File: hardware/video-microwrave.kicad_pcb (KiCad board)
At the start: 2 copper layers, 66 x 101.6 mm, 85 parts, among them J501 PJ301M-12, J502 PJ301M-12, J503 PJ301M-12, J504 PJ301M-12, J505 PJ301M-12, J506 PJ301M-12, J507 PJ301M-12, J508 PJ301M-12, P101 CONN_01X05, P102 CONN_01X05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

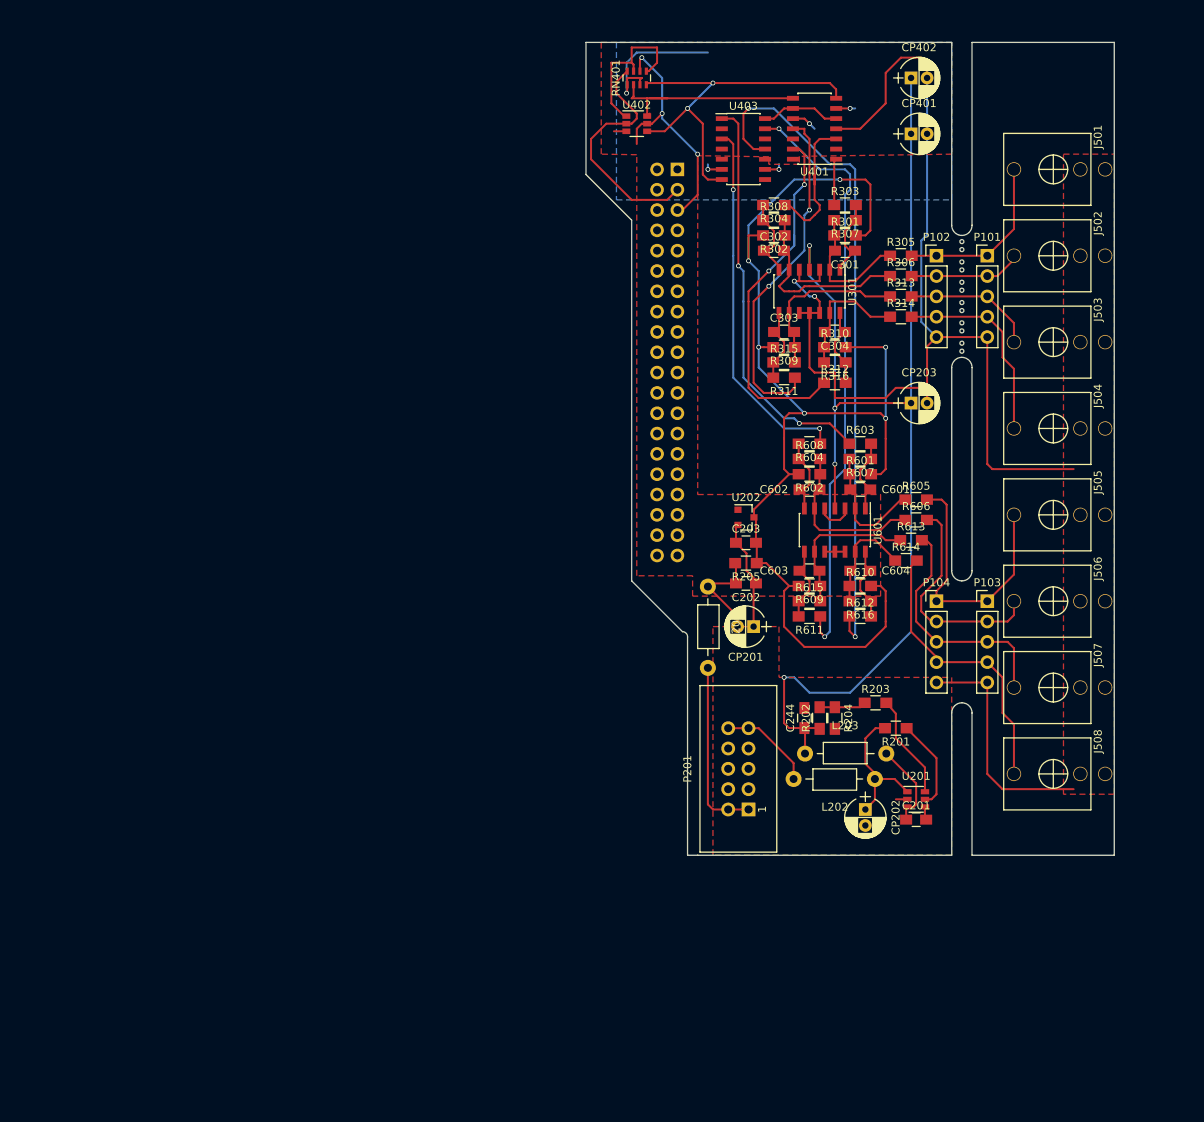
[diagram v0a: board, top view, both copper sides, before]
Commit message: moving footprints to fit real world dimensions
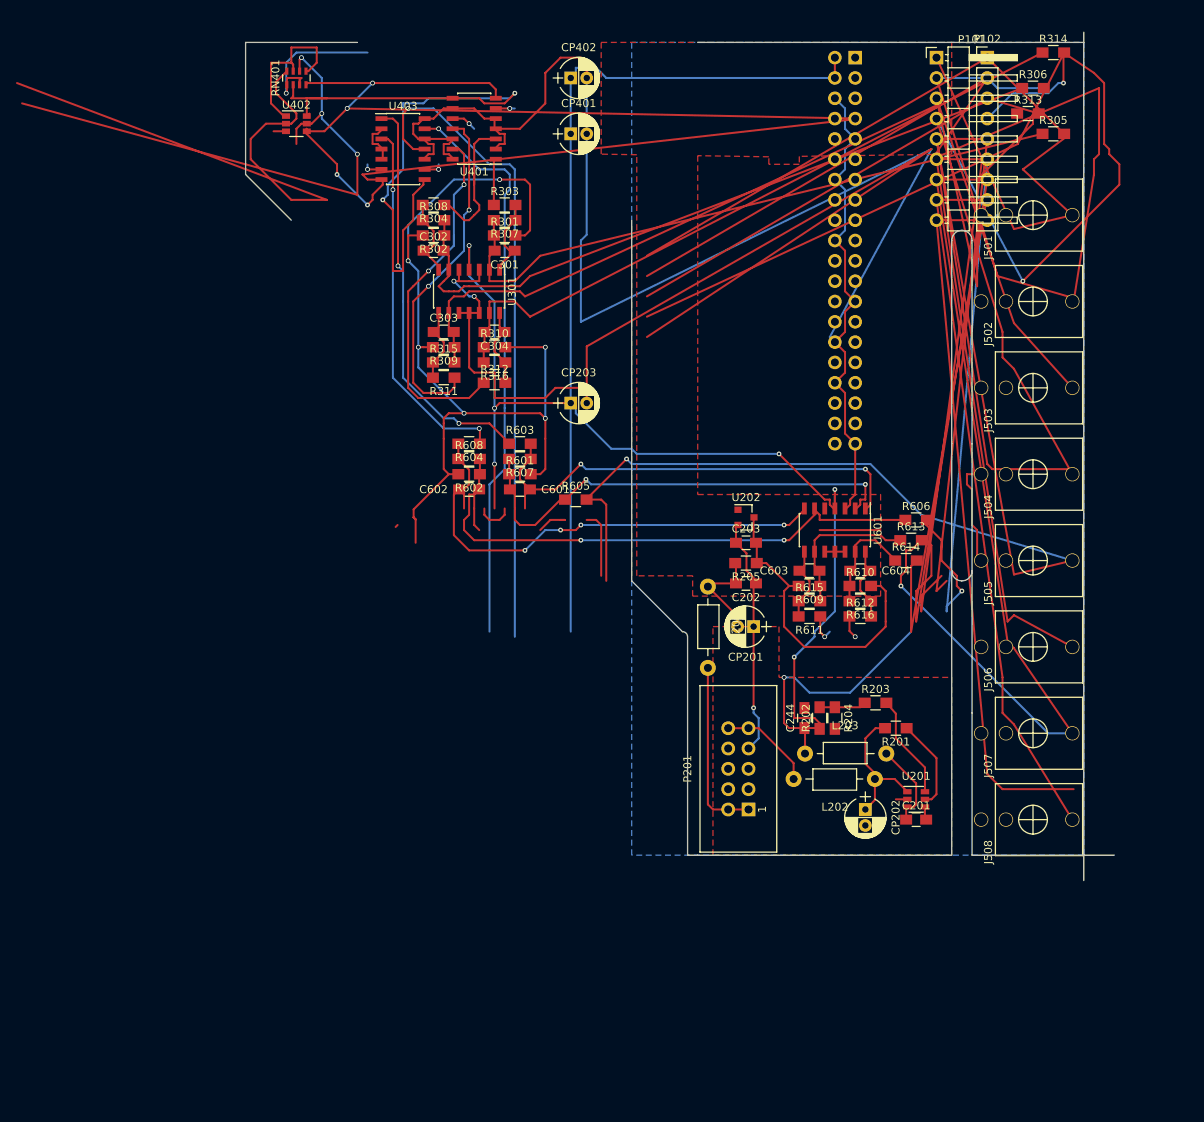
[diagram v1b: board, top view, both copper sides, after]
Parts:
- removed MOUSEBITE1mm (x6): VAL**, Microwrave:Mousebite_Mini_1mm
- removed P103, P104: CONN_01X05, Pin_Headers:Pin_Header_Straight_1x05_Pitch2.54mm
- P101: value CONN_01X05 -> CONN_01X09; footprint Pin_Headers:Pin_Header_Straight_1x05_Pitch2.54mm -> Pin_Headers:Pin_Header_Angled_1x09_Pitch2.54mm
- P102: value CONN_01X05 -> CONN_01X09; footprint Pin_Headers:Pin_Header_Straight_1x05_Pitch2.54mm -> Pin_Headers:Pin_Header_Straight_1x09_Pitch2.54mm
- moved C302 42.5 mm to (87.6, 64.1)
- moved R302 42.5 mm to (87.6, 62.2)
- moved R304 42.5 mm to (87.6, 58.4)
- moved R308 42.5 mm to (87.6, 60.3)
- moved R605 42.5 mm to (105.4, 95.2)
- moved C301 42.5 mm to (96.5, 64.1)
- moved C601 42.5 mm to (98.4, 94.0)
- moved C602 42.5 mm to (92.1, 94.0)
- moved R301 42.5 mm to (96.5, 62.2)
- moved R303 42.5 mm to (96.5, 58.4)
- moved R307 42.5 mm to (96.5, 60.3)
- moved R601 42.5 mm to (98.4, 92.1)
- moved R602 42.5 mm to (92.1, 92.1)
- moved R603 42.5 mm to (98.4, 88.3)
- moved R604 42.5 mm to (92.1, 88.3)
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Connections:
- P101 pad 5: Earth -> /cv5_raw
- P102 pad 5: Earth -> /cv5_raw
- U101 pad 10: Net-(U101-Pad10) -> (no net)
- U101 pad 11: Net-(U101-Pad11) -> (no net)
- U101 pad 12: Net-(U101-Pad12) -> (no net)
- U101 pad 13: Net-(U101-Pad13) -> (no net)
- U101 pad 15: Net-(U101-Pad15) -> (no net)
- U101 pad 16: Net-(U101-Pad16) -> (no net)
- U101 pad 17: Net-(U101-Pad17) -> (no net)
- U101 pad 18: Net-(U101-Pad18) -> (no net)
- U101 pad 19: Net-(U101-Pad19) -> (no net)
- U101 pad 21: Net-(U101-Pad21) -> (no net)
- U101 pad 22: Net-(U101-Pad22) -> (no net)
- U101 pad 23: Net-(U101-Pad23) -> (no net)
- U101 pad 24: Net-(U101-Pad24) -> (no net)
- U101 pad 26: Net-(U101-Pad26) -> (no net)
- U101 pad 27: Net-(U101-Pad27) -> (no net)
- U101 pad 28: Net-(U101-Pad28) -> (no net)
- U101 pad 29: Net-(U101-Pad29) -> (no net)
- U101 pad 31: Net-(U101-Pad31) -> (no net)
- U101 pad 32: Net-(U101-Pad32) -> (no net)
- U101 pad 33: Net-(U101-Pad33) -> (no net)
- U101 pad 35: Net-(U101-Pad35) -> (no net)
- U101 pad 36: Net-(U101-Pad36) -> (no net)
- U101 pad 37: Net-(U101-Pad37) -> (no net)
- U101 pad 38: Net-(U101-Pad38) -> (no net)
- U101 pad 40: Net-(U101-Pad40) -> (no net)
- U101 pad 7: Net-(U101-Pad7) -> (no net)
- U101 pad 8: Net-(U101-Pad8) -> (no net)
- U202 pad 1: Net-(U202-Pad1) -> (no net)
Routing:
- net Earth: track 197.4 -> 505.3 mm, vias 2 -> 3
- net /cv6_raw: track 28.1 -> 243.3 mm, vias 0 -> 1
- net /cv5_raw: track 33.8 -> 247.9 mm, vias 0 -> 1
- net /cv3_raw: track 16.5 -> 202.7 mm
- net /cv4_raw: track 24.8 -> 198.5 mm, vias 0 -> 2
- net /cv7_raw: track 30.3 -> 181.7 mm, vias 0 -> 1
- net /adc/SDA_5V: track 47.7 -> 182.5 mm, vias 2 -> 4
- net /cv8_raw: track 36.0 -> 152.3 mm
- net +5V: track 179.2 -> 292.9 mm, vias 9 -> 12
- net /cv2_raw: track 14.1 -> 126.6 mm
- net /cv1_raw: track 21.6 -> 109.3 mm
- net Net-(C304-Pad2): track 16.3 -> 85.9 mm
- net Net-(C301-Pad2): track 16.8 -> 80.2 mm
- net Net-(C302-Pad2): track 24.3 -> 87.7 mm
- net /adc/SCL_5V: track 26.8 -> 86.4 mm, vias 0 -> 2
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- added copper zone on F.Cu, net +5V
- added copper zone on B.Cu, net Earth
- removed copper zone on B.Cu, net +5V
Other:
- board size 66 x 101.6 mm -> 108.6 x 106 mm

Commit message: made space for an expansion connector. net needs updating for 8 100k resistors coming from raw signals
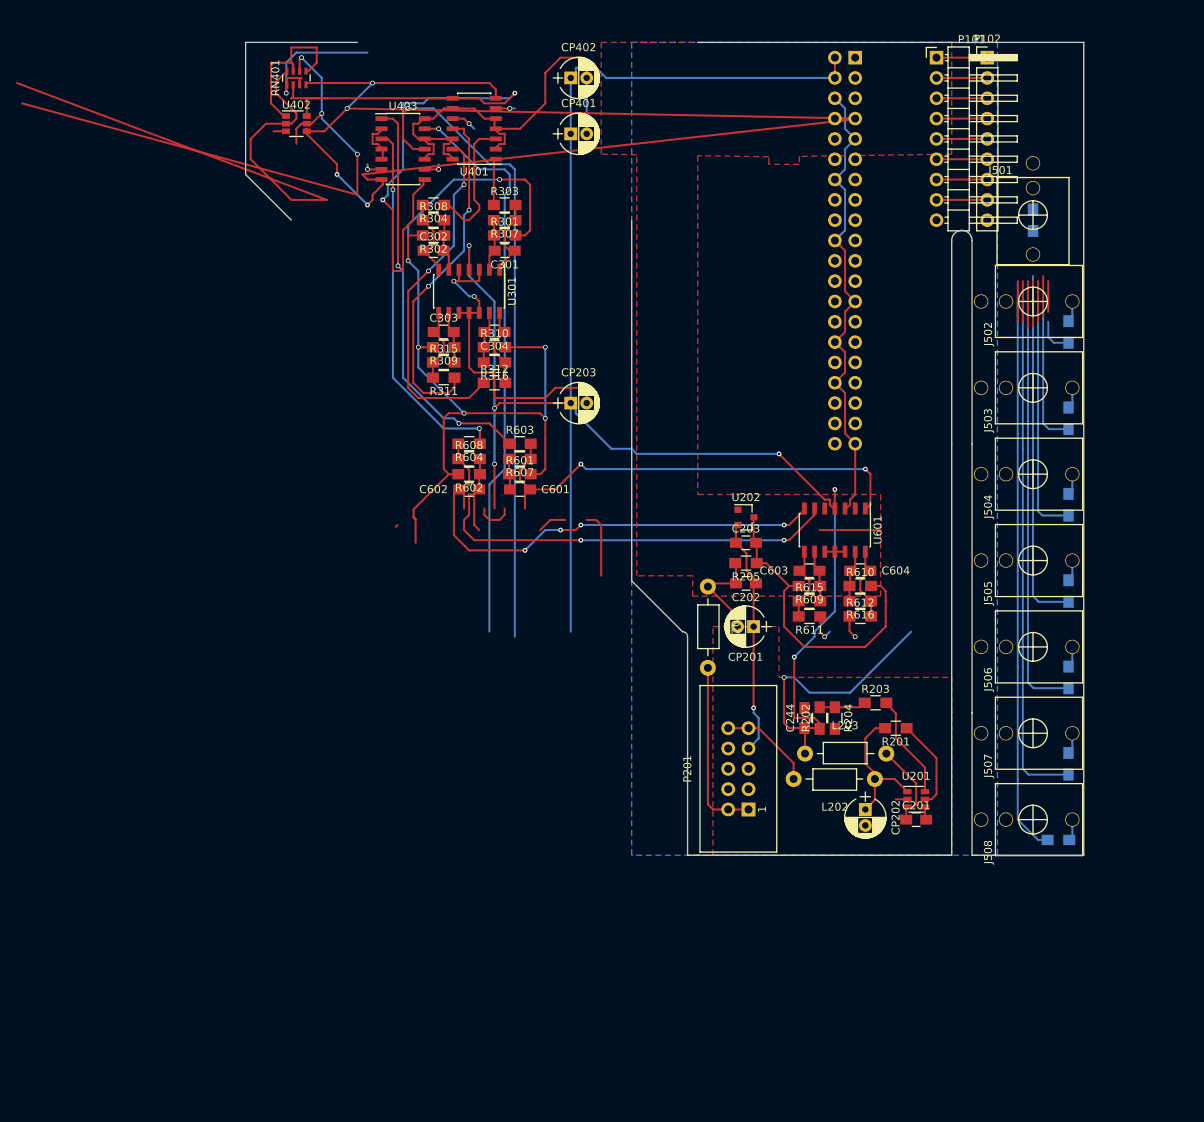
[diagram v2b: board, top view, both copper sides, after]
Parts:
- R305, R306, R313, R314, R605, R606, R613, R614: moved to B.Cu
- moved R605 62.6 mm to (167.0, 106.7), turned to 90 degrees
- moved R314 56.5 mm to (167.0, 95.9), turned to 90 degrees
- moved R614 39.8 mm to (165.7, 137.8)
- moved R313 38.4 mm to (167.0, 85.1), turned to 90 degrees
- moved R613 34.2 mm to (167.0, 128.3), turned to 90 degrees
- moved R306 30.8 mm to (167.0, 74.3), turned to 90 degrees
- moved R606 27.4 mm to (167.0, 117.5), turned to 90 degrees
- moved R305 11.1 mm to (162.6, 60.3), turned to 270 degrees
- turned J501 to 180 degrees
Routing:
- net Earth: track 505.3 -> 201.9 mm
- net /cv5_raw: track 247.9 -> 9.57 mm, vias 1 -> 0
- net /cv6_raw: track 243.3 -> 9.64 mm, vias 1 -> 0
- net /cv3_raw: track 202.7 -> 9.57 mm
- net /cv4_raw: track 198.5 -> 9.01 mm, vias 2 -> 0
- net /cv7_raw: track 181.7 -> 9.57 mm, vias 1 -> 0
- net /cv8_raw: track 152.3 -> 9.80 mm
- net /cv2_raw: track 126.6 -> 9.73 mm
- net /cv1_raw: track 109.3 -> 6.35 mm
- net Net-(C302-Pad2): track 87.7 -> 11.5 mm
- net Net-(C301-Pad2): track 80.2 -> 6.50 mm
- net Net-(C604-Pad2): track 13.6 -> 76.0 mm
- net Net-(C603-Pad2): track 19.2 -> 71.6 mm
- net Net-(C304-Pad2): track 85.9 -> 34.9 mm
- net Net-(C602-Pad2): track 74.6 -> 115.3 mm
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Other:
- board size 108.6 x 106 mm -> 104.8 x 101.6 mm

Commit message: reworked input board
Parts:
- added EXPANDER501: CONN_02X05, Pin_Headers:Pin_Header_Straight_2x05_Pitch2.54mm, F.Cu at (162.6, 40.0)
- R305, R306, R313, R314, R605, R606, R613, R614: moved to F.Cu
- moved R614 81.8 mm to (148.6, 57.8)
- moved C603 77.0 mm to (84.5, 162.6)
- moved R609 77.0 mm to (84.5, 164.5)
- moved R611 77.0 mm to (84.5, 168.3)
- moved R615 77.0 mm to (84.5, 166.4)
- moved R610 77.0 mm to (90.8, 164.5)
- moved R612 77.0 mm to (90.8, 168.3)
- moved R616 77.0 mm to (90.8, 166.4)
- moved U601 75.9 mm to (101.6, 165.7), turned to 0 degrees
- moved R613 75.3 mm to (148.6, 55.2), turned to 0 degrees
- moved R606 67.3 mm to (148.6, 52.7), turned to 0 degrees
- moved R607 67.3 mm to (99.7, 157.5), turned to 0 degrees
- moved C604 66.4 mm to (104.1, 159.4)
- moved R603 66.0 mm to (98.4, 154.3), turned to 270 degrees
- moved C601 65.4 mm to (99.7, 159.4), turned to 0 degrees
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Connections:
- J501 pad 2: Earth -> /CV jacks/expansion1
- J502 pad 2: Earth -> /CV jacks/expansion2
- J503 pad 2: Earth -> /CV jacks/expansion3
- J504 pad 2: Earth -> /CV jacks/expansion4
- J505 pad 2: Earth -> /CV jacks/expansion5
- J506 pad 2: Earth -> /CV jacks/expansion6
- J507 pad 2: Earth -> /CV jacks/expansion7
- J508 pad 2: Earth -> /CV jacks/expansion8
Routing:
- net (no net): track 60.8 -> 234.0 mm, vias 0 -> 5
- net /adc/SDA_5V: track 182.5 -> 53.1 mm
- net Net-(C602-Pad2): track 115.3 -> 11.6 mm, vias 2 -> 0
- net /CV jacks/expansion8: track 0.00 -> 102.2 mm
- net +5V: track 292.9 -> 190.8 mm, vias 12 -> 8
- net /CV jacks/expansion7: track 0.00 -> 87.7 mm
- net /cv8_raw: track 9.80 -> 90.4 mm
- net /CV jacks/expansion6: track 0.00 -> 73.9 mm
- net /cv7_raw: track 9.57 -> 81.4 mm
- net Net-(C604-Pad2): track 76.0 -> 10.5 mm
- net /power/-12: track 22.4 -> 87.8 mm
- net /cv6_raw: track 9.64 -> 73.3 mm
- net Net-(C603-Pad2): track 71.6 -> 8.81 mm
- net Net-(C602-Pad1): track 62.7 -> 0.00 mm, vias 4 -> 0
- net /CV jacks/expansion5: track 0.00 -> 59.4 mm
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- removed copper zone on F.Cu, net +5V
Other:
- outline, holes or cut-outs redrawn

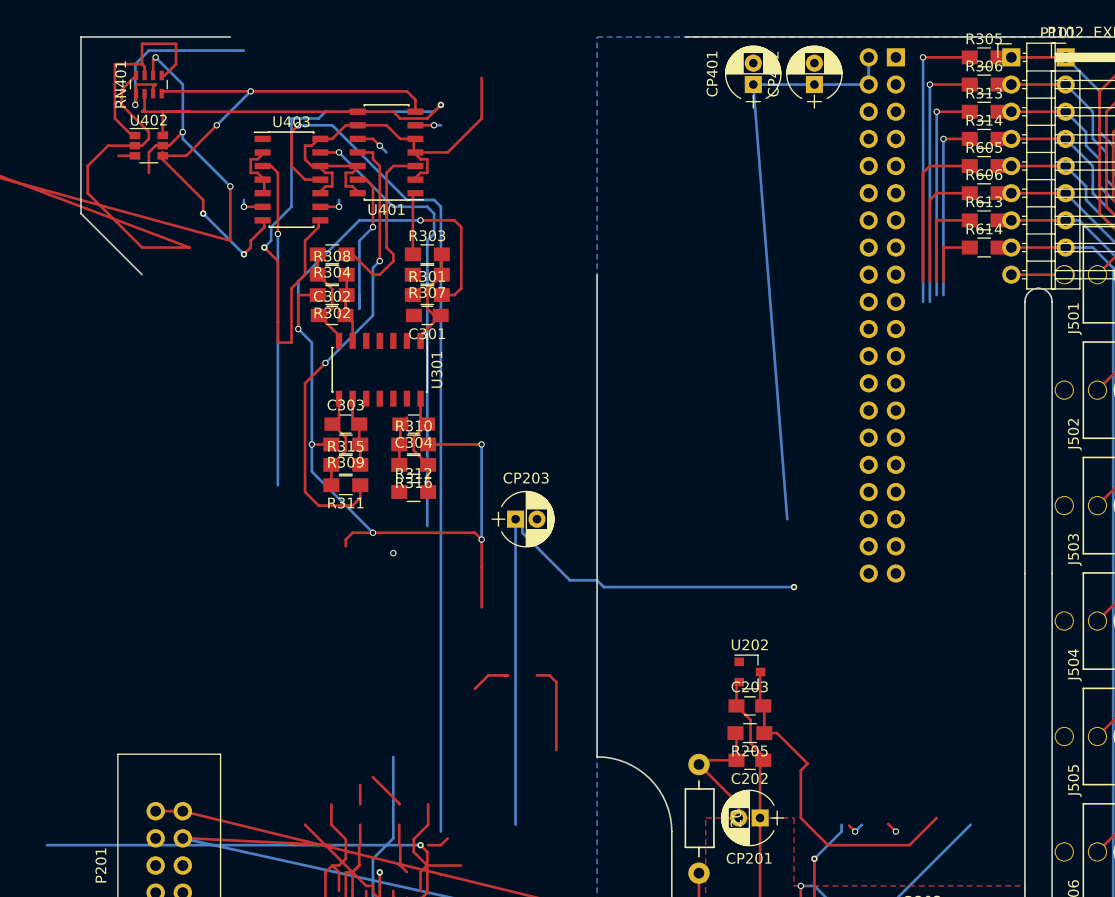
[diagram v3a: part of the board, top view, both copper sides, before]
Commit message: shoved op amp into 1cm space
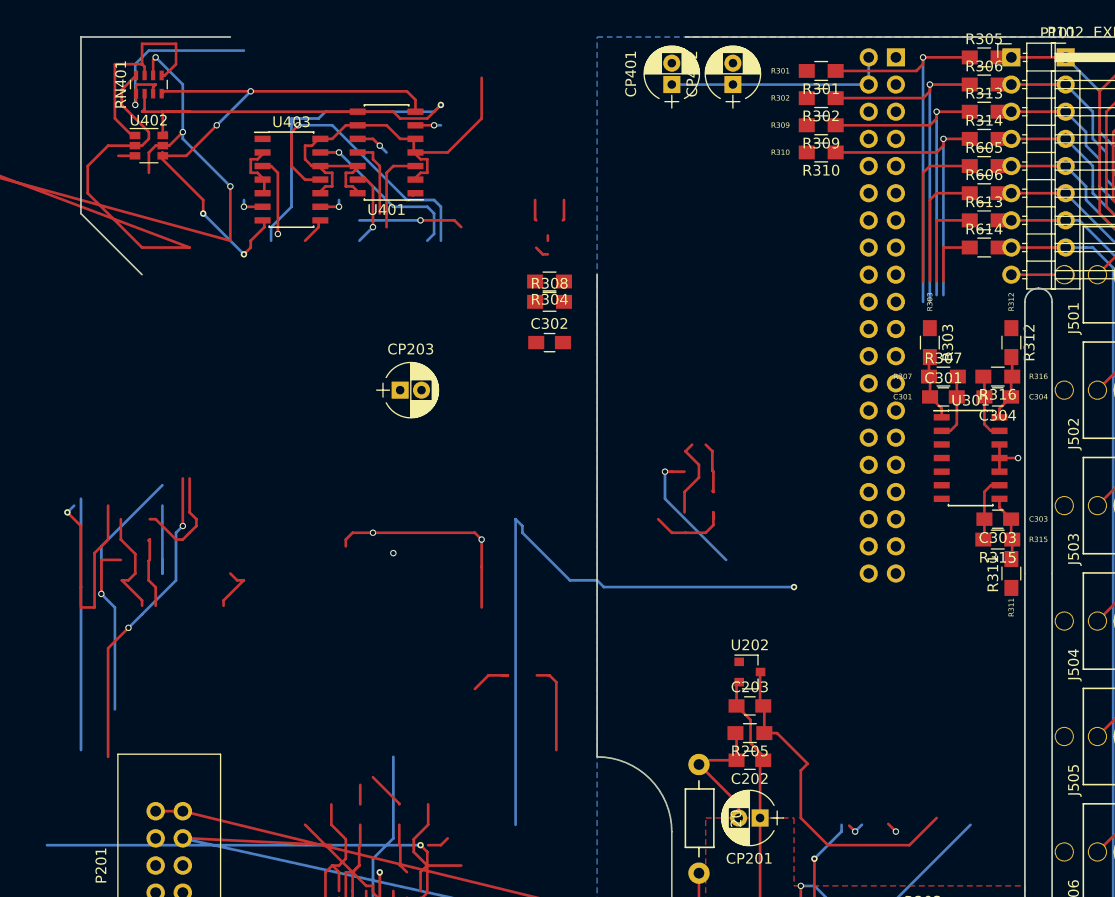
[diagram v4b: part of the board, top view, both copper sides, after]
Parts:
- moved R311 62.8 mm to (151.1, 88.3), turned to 90 degrees
- moved C303 61.6 mm to (149.9, 83.2), turned to 180 degrees
- moved R315 61.4 mm to (149.9, 85.1), turned to 180 degrees
- moved R312 57.6 mm to (151.1, 66.7), turned to 270 degrees
- moved U301 55.9 mm to (147.3, 77.5), turned to 0 degrees
- moved R316 55.2 mm to (149.9, 69.8)
- moved C304 54.7 mm to (149.9, 71.8)
- moved R309 53.5 mm to (133.3, 46.4)
- moved R302 49.3 mm to (133.3, 43.8)
- moved R307 49.2 mm to (144.8, 69.8), turned to 0 degrees
- moved C301 48.9 mm to (144.8, 71.8), turned to 0 degrees
- moved R303 47.7 mm to (143.5, 66.7), turned to 270 degrees
- moved R310 46.9 mm to (133.3, 48.9), turned to 180 degrees
- moved R301 42.4 mm to (133.3, 41.3), turned to 180 degrees
- moved C302 20.5 mm to (108.0, 66.7)
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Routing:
- net (no net): track 234.0 -> 502.8 mm, vias 5 -> 14
- net /buffers 1-4/-5V: track 125.1 -> 32.1 mm, vias 6 -> 0
- net +5V: track 190.8 -> 100.0 mm, vias 8 -> 7
- net /buffered_8: track 82.2 -> 27.0 mm
- net /buffered_3: track 44.1 -> 7.41 mm, vias 2 -> 0
- net /buffered_7: track 42.5 -> 15.8 mm
- net /buffered_6: track 30.9 -> 7.41 mm
- net /adc/SCL_5V: track 86.4 -> 64.7 mm, vias 2 -> 1
- net Net-(C301-Pad2): track 27.2 -> 42.6 mm
- net Net-(C304-Pad2): track 21.8 -> 34.3 mm
- net /buffered_2: track 18.4 -> 8.04 mm
- net Net-(C302-Pad1): track 10.3 -> 0.00 mm
- net Net-(C303-Pad2): track 26.9 -> 36.9 mm
- net /buffered_4: track 15.0 -> 7.30 mm
- net /buffered_1: track 5.81 -> 0.34 mm
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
